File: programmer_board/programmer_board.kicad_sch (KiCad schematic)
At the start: 14 parts, among them J1 8bit_thing_bus_connector, J2 greenpak_i2c, U1 Pico, U2 74AHCT573, U3 74AHCT573, U4 74AHCT573, U5 74LVC245, U6 SLG46826G

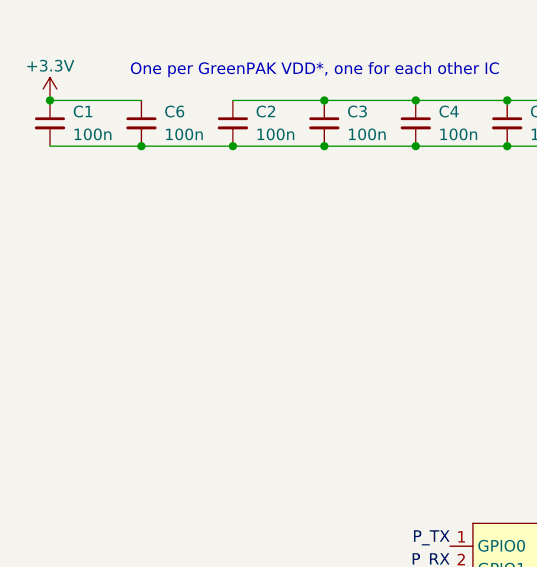
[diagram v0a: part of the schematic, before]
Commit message: pico board: add more bypass caps, add JLCPCB string
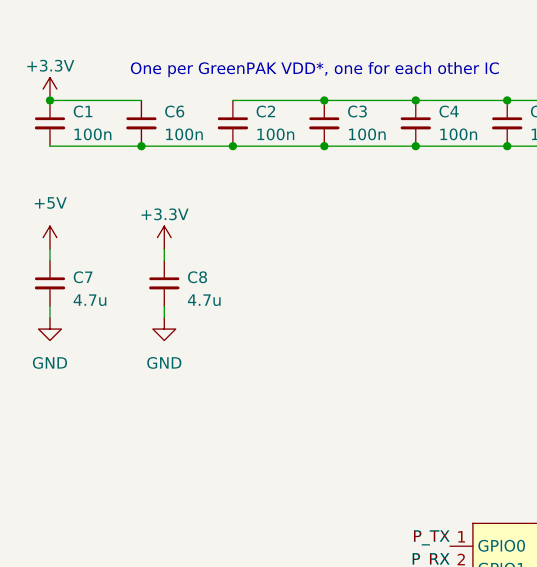
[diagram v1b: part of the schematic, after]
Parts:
- added C7, C8: 4.7u, Capacitor_SMD:C_0805_2012Metric_Pad1.18x1.45mm_HandSolder, symbol Device:C_Small
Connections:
- net +3.3V: now also C8.1
- net +5V: now also C7.1
- net GND: now also C7.2, C8.2
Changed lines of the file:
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@@
+    (stroke (width 0) (type default))
+  )
+  (wire (pts (xy 34.29 50.8) (xy 34.29 49.53))
     (stroke (width 0) (type default))
   )
@@
     (stroke (width 0) (type default))
   )
+  (wire (pts (xy 34.29 43.18) (xy 34.29 44.45))
+    (stroke (width 0) (type default))
+  )
   (wire (pts (xy 236.22 107.95) (xy 241.3 107.95))
     (stroke (width 0) (type default))
@@
     (stroke (width 0) (type default))
   )
+  (wire (pts (xy 21.59 50.8) (xy 21.59 49.53))
+    (stroke (width 0) (type default))
+  )
   (bus (pts (xy 222.25 109.22) (xy 222.25 106.68))
     (stroke (width 0) (type default))
@@
   )
   (wire (pts (xy 236.22 92.71) (xy 241.3 92.71))
+    (stroke (width 0) (type default))
+  )
+  (wire (pts (xy 21.59 43.18) (xy 21.59 44.45))
     (stroke (width 0) (type default))
   )
@@
     )
   )
+  (symbol (lib_id "power:+5V") (at 21.59 43.18 0) (unit 1)
+    (in_bom yes) (on_board yes) (dnp no) (fields_autoplaced)
+    (property "Reference" "#PWR025" (at 21.59 46.99 0)
+      (effects (font (size 1.27 1.27)) hide)
+    )
+    (property "Value" "+5V" (at 21.59 38.1 0)
+      (effects (font (size 1.27 1.27)))
+    )
+    (property "Footprint" "" (at 21.59 43.18 0)
+      (effects (font (size 1.27 1.27)) hide)
+    )
+    (property "Datasheet" "" (at 21.59 43.18 0)
+      (effects (font (size 1.27 1.27)) hide)
+    )
+    (pin "1")
+    (instances
+      (project "programmer_board"
+        (path "/d80ca4e7-5430-4474-aabd-9f00c61eaf5c"
+          (reference "#PWR025") (unit 1)
+        )
+      )
+      (project "HD6301V1_thing"
+        (path "/f94fb884-8365-431c-b8b6-ec4493810111"
+          (reference "#PWR031") (unit 1)
+        )
+      )
+    )
+  )
   (symbol (lib_id "power:GND") (at 203.2 121.92 0) (unit 1)
     (in_bom yes) (on_board yes) (dnp no)
@@
     )
   )
+  (symbol (lib_id "Device:C_Small") (at 21.59 46.99 0) (unit 1)
+    (in_bom yes) (on_board yes) (dnp no) (fields_autoplaced)
+    (property "Reference" "C7" (at 24.13 46.3613 0)
+      (effects (font (size 1.27 1.27)) (justify left))
+    )
+    (property "Value" "4.7u" (at 24.13 48.9013 0)
+      (effects (font (size 1.27 1.27)) (justify left))
+    )
+    (property "Footprint" "Capacitor_SMD:C_0805_2012Metric_Pad1.18x1.45mm_HandSolder" (at 21.59 46.99 0)
+      (effects (font (size 1.27 1.27)) hide)
+    )
+    (property "Datasheet" "~" (at 21.59 46.99 0)
+      (effects (font (size 1.27 1.27)) hide)
+    )
+    (pin "1")
+    (pin "2")
+    (instances
+      (project "programmer_board"
+        (path "/d80ca4e7-5430-4474-aabd-9f00c61eaf5c"
+          (reference "C7") (unit 1)
+        )
+      )
+      (project "HD6301V1_thing"
+        (path "/f94fb884-8365-431c-b8b6-ec4493810111"
+          (reference "C5") (unit 1)
+        )
+      )
+    )
+  )
   (symbol (lib_id "power:GND") (at 180.34 157.48 0) (unit 1)
     (in_bom yes) (on_board yes) (dnp no)
@@
     )
   )
+  (symbol (lib_id "Device:C_Small") (at 34.29 46.99 0) (unit 1)
+    (in_bom yes) (on_board yes) (dnp no) (fields_autoplaced)
+    (property "Reference" "C8" (at 36.83 46.3613 0)
+      (effects (font (size 1.27 1.27)) (justify left))
+    )
+    (property "Value" "4.7u" (at 36.83 48.9013 0)
+      (effects (font (size 1.27 1.27)) (justify left))
+    )
+    (property "Footprint" "Capacitor_SMD:C_0805_2012Metric_Pad1.18x1.45mm_HandSolder" (at 34.29 46.99 0)
+      (effects (font (size 1.27 1.27)) hide)
+    )
+    (property "Datasheet" "~" (at 34.29 46.99 0)
+      (effects (font (size 1.27 1.27)) hide)
+    )
+    (pin "1")
+    (pin "2")
+    (instances
+      (project "programmer_board"
+        (path "/d80ca4e7-5430-4474-aabd-9f00c61eaf5c"
+          (reference "C8") (unit 1)
+        )
+      )
+      (project "HD6301V1_thing"
+        (path "/f94fb884-8365-431c-b8b6-ec4493810111"
+          (reference "C5") (unit 1)
+        )
+      )
+    )
+  )
   (symbol (lib_id "power:GND") (at 154.94 66.04 0) (unit 1)
     (in_bom yes) (on_board yes) (dnp no) (fields_autoplaced)
@@
         (path "/d80ca4e7-5430-4474-aabd-9f00c61eaf5c"
           (reference "#PWR016") (unit 1)
+        )
+      )
+    )
+  )
+  (symbol (lib_id "power:+3.3V") (at 34.29 43.18 0) (unit 1)
+    (in_bom yes) (on_board yes) (dnp no) (fields_autoplaced)
+    (property "Reference" "#PWR024" (at 34.29 46.99 0)
+      (effects (font (size 1.27 1.27)) hide)
+    )
+    (property "Value" "+3.3V" (at 34.29 39.37 0)
+      (effects (font (size 1.27 1.27)))
+    )
+    (property "Footprint" "" (at 34.29 43.18 0)
+      (effects (font (size 1.27 1.27)) hide)
+    )
+    (property "Datasheet" "" (at 34.29 43.18 0)
+      (effects (font (size 1.27 1.27)) hide)
+    )
+    (pin "1")
+    (instances
+      (project "programmer_board"
+        (path "/d80ca4e7-5430-4474-aabd-9f00c61eaf5c"
+          (reference "#PWR024") (unit 1)
         )
       )
@@
     )
   )
+  (symbol (lib_id "power:GND") (at 34.29 50.8 0) (unit 1)
+    (in_bom yes) (on_board yes) (dnp no) (fields_autoplaced)
+    (property "Reference" "#PWR027" (at 34.29 57.15 0)
+      (effects (font (size 1.27 1.27)) hide)
+    )
+    (property "Value" "GND" (at 34.29 55.88 0)
+      (effects (font (size 1.27 1.27)))
+    )
+    (property "Footprint" "" (at 34.29 50.8 0)
+      (effects (font (size 1.27 1.27)) hide)
+    )
+    (property "Datasheet" "" (at 34.29 50.8 0)
+      (effects (font (size 1.27 1.27)) hide)
+    )
+    (pin "1")
+    (instances
+      (project "programmer_board"
+        (path "/d80ca4e7-5430-4474-aabd-9f00c61eaf5c"
+          (reference "#PWR027") (unit 1)
+        )
+      )
+      (project "HD6301V1_thing"
+        (path "/f94fb884-8365-431c-b8b6-ec4493810111"
+          (reference "#PWR032") (unit 1)
+        )
+      )
+    )
+  )
   (symbol (lib_id "power:+5V") (at 104.14 66.04 0) (unit 1)
     (in_bom yes) (on_board yes) (dnp no) (fields_autoplaced)
@@
         )
       )
+    )
+  )
+  (symbol (lib_id "power:GND") (at 21.59 50.8 0) (unit 1)
+    (in_bom yes) (on_board yes) (dnp no) (fields_autoplaced)
+    (property "Reference" "#PWR026" (at 21.59 57.15 0)
+      (effects (font (size 1.27 1.27)) hide)
+    )
+    (property "Value" "GND" (at 21.59 55.88 0)
+      (effects (font (size 1.27 1.27)))
+    )
+    (property "Footprint" "" (at 21.59 50.8 0)
+      (effects (font (size 1.27 1.27)) hide)
+    )
+    (property "Datasheet" "" (at 21.59 50.8 0)
+      (effects (font (size 1.27 1.27)) hide)
+    )
+    (pin "1")
+    (instances
+      (project "programmer_board"
+        (path "/d80ca4e7-5430-4474-aabd-9f00c61eaf5c"
+          (reference "#PWR026") (unit 1)
+        )
+      )
+      (project "HD6301V1_thing"
+        (path "/f94fb884-8365-431c-b8b6-ec4493810111"
+          (reference "#PWR032") (unit 1)
+        )
+      )

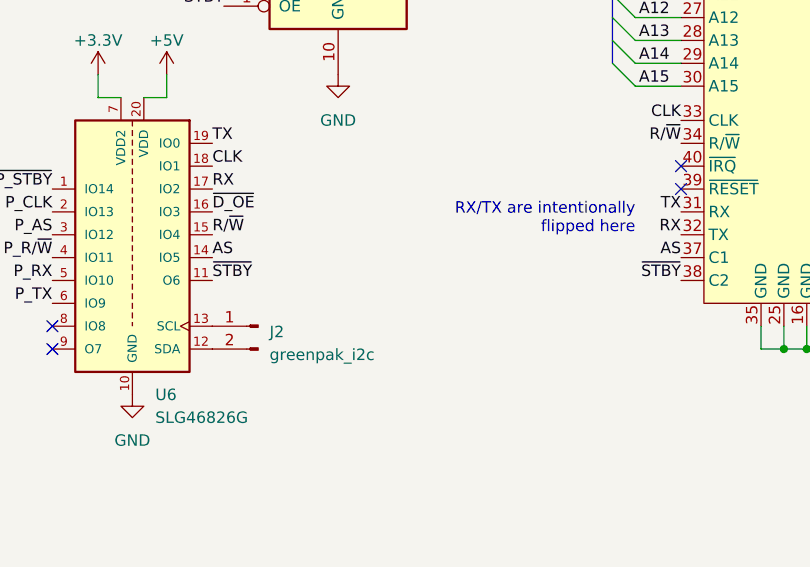
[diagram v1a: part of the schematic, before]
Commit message: Pico board: add i2c pullups
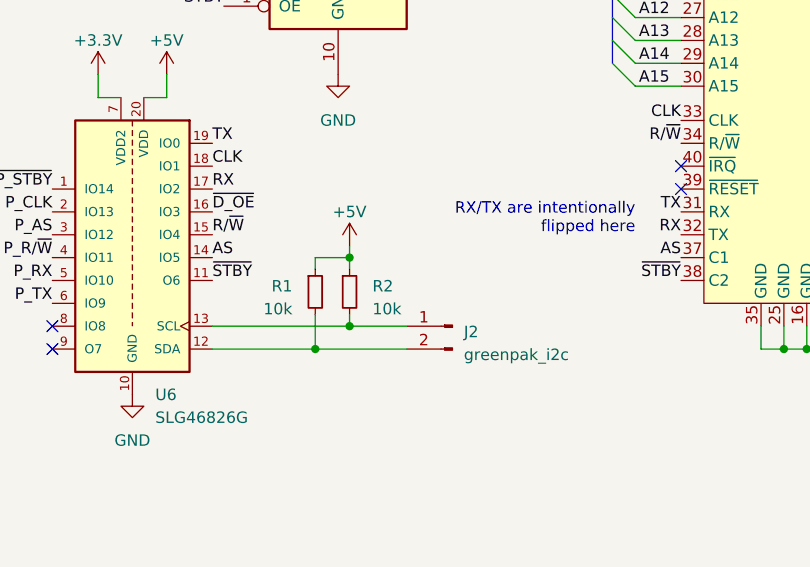
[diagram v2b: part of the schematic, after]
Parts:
- added R1, R2: 10k, Resistor_SMD:R_0805_2012Metric_Pad1.20x1.40mm_HandSolder, symbol Device:R_Small
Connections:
- net +5V: now also R1.1, R2.1
- net at J2.1 (Pin_1), U6.13 (SCL): now also R2.2
- net at J2.2 (Pin_2), U6.12 (SDA): now also R1.2
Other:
- moved on the sheet: J2
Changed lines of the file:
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@@
   (junction (at 110.49 106.68) (diameter 0) (color 0 0 0 0)
   )
+  (junction (at 204.47 142.24) (diameter 0) (color 0 0 0 0)
+  )
   (junction (at 62.23 31.75) (diameter 0) (color 0 0 0 0)
   )
@@
   (junction (at 257.81 152.4) (diameter 0) (color 0 0 0 0)
   )
+  (junction (at 204.47 149.86) (diameter 0) (color 0 0 0 0)
+  )
   (junction (at 52.07 31.75) (diameter 0) (color 0 0 0 0)
   )
   (junction (at 110.49 93.98) (diameter 0) (color 0 0 0 0)
+  )
+  (junction (at 200.66 152.4) (diameter 0) (color 0 0 0 0)
   )
   (junction (at 72.39 31.75) (diameter 0) (color 0 0 0 0)
@@
     (stroke (width 0) (type default))
   )
+  (wire (pts (xy 200.66 142.24) (xy 204.47 142.24))
+    (stroke (width 0) (type default))
+  )
   (wire (pts (xy 236.22 66.04) (xy 241.3 66.04))
     (stroke (width 0) (type default))
@@
     (stroke (width 0) (type default))
   )
+  (wire (pts (xy 204.47 148.59) (xy 204.47 149.86))
+    (stroke (width 0) (type default))
+  )
   (wire (pts (xy 48.26 119.38) (xy 48.26 130.81))
     (stroke (width 0) (type default))
   )
+  (wire (pts (xy 204.47 142.24) (xy 204.47 143.51))
+    (stroke (width 0) (type default))
+  )
   (wire (pts (xy 139.7 57.15) (xy 142.24 57.15))
     (stroke (width 0) (type default))
@@
     (stroke (width 0) (type default))
   )
+  (wire (pts (xy 200.66 143.51) (xy 200.66 142.24))
+    (stroke (width 0) (type default))
+  )
   (wire (pts (xy 104.14 78.74) (xy 104.14 76.2))
     (stroke (width 0) (type default))
@@
     (stroke (width 0) (type default))
   )
+  (wire (pts (xy 210.82 149.86) (xy 204.47 149.86))
+    (stroke (width 0) (type default))
+  )
   (bus (pts (xy 173.99 106.68) (xy 173.99 104.14))
     (stroke (width 0) (type default))
@@
     (stroke (width 0) (type default))
   )
+  (wire (pts (xy 210.82 152.4) (xy 200.66 152.4))
+    (stroke (width 0) (type default))
+  )
   (wire (pts (xy 236.22 78.74) (xy 241.3 78.74))
     (stroke (width 0) (type default))
@@
     (stroke (width 0) (type default))
   )
+  (wire (pts (xy 200.66 152.4) (xy 189.23 152.4))
+    (stroke (width 0) (type default))
+  )
   (bus (pts (xy 233.68 115.57) (xy 233.68 118.11))
     (stroke (width 0) (type default))
@@
     (stroke (width 0) (type default))
   )
+  (wire (pts (xy 200.66 148.59) (xy 200.66 152.4))
+    (stroke (width 0) (type default))
+  )
   (wire (pts (xy 219.71 99.06) (xy 215.9 99.06))
     (stroke (width 0) (type default))
@@
     (stroke (width 0) (type default))
   )
+  (wire (pts (xy 204.47 149.86) (xy 189.23 149.86))
+    (stroke (width 0) (type default))
+  )
   (wire (pts (xy 171.45 41.91) (xy 167.64 41.91))
     (stroke (width 0) (type default))
@@
   )
   (wire (pts (xy 48.26 106.68) (xy 48.26 119.38))
+    (stroke (width 0) (type default))
+  )
+  (wire (pts (xy 204.47 140.97) (xy 204.47 142.24))
     (stroke (width 0) (type default))
   )
@@
     )
   )
-  (symbol (lib_id "Connector:Conn_01x02_Pin") (at 194.31 149.86 0) (mirror y) (unit 1)
+  (symbol (lib_id "Connector:Conn_01x02_Pin") (at 215.9 149.86 0) (mirror y) (unit 1)
     (in_bom yes) (on_board yes) (dnp no)
-    (property "Reference" "J2" (at 195.58 150.495 0)
+    (property "Reference" "J2" (at 217.17 150.495 0)
       (effects (font (size 1.27 1.27)) (justify right))
     )
-    (property "Value" "greenpak_i2c" (at 195.58 153.035 0)
+    (property "Value" "greenpak_i2c" (at 217.17 153.035 0)
       (effects (font (size 1.27 1.27)) (justify right))
     )
-    (property "Footprint" "own_footprints:PinHeader_1x02_P2.54mm_Vertical_minimal" (at 194.31 149.86 0)
-      (effects (font (size 1.27 1.27)) hide)
-    )
-    (property "Datasheet" "~" (at 194.31 149.86 0)
+    (property "Footprint" "own_footprints:PinHeader_1x02_P2.54mm_Vertical_minimal" (at 215.9 149.86 0)
+      (effects (font (size 1.27 1.27)) hide)
+    )
+    (property "Datasheet" "~" (at 215.9 149.86 0)
       (effects (font (size 1.27 1.27)) hide)
     )
@@
     )
   )
+  (symbol (lib_id "Device:R_Small") (at 200.66 146.05 0) (unit 1)
+    (in_bom yes) (on_board yes) (dnp no) (fields_autoplaced)
+    (property "Reference" "R1" (at 198.12 145.415 0)
+      (effects (font (size 1.27 1.27)) (justify right))
+    )
+    (property "Value" "10k" (at 198.12 147.955 0)
+      (effects (font (size 1.27 1.27)) (justify right))
+    )
+    (property "Footprint" "Resistor_SMD:R_0805_2012Metric_Pad1.20x1.40mm_HandSolder" (at 200.66 146.05 0)
+      (effects (font (size 1.27 1.27)) hide)
+    )
+    (property "Datasheet" "~" (at 200.66 146.05 0)
+      (effects (font (size 1.27 1.27)) hide)
+    )
+    (pin "1")
+    (pin "2")
+    (instances
+      (project "programmer_board"
+        (path "/d80ca4e7-5430-4474-aabd-9f00c61eaf5c"
+          (reference "R1") (unit 1)
+        )
+      )
+    )
+  )
   (symbol (lib_id "power:GND") (at 83.82 33.02 0) (unit 1)
     (in_bom yes) (on_board yes) (dnp no) (fields_autoplaced)
@@
         (path "/d80ca4e7-5430-4474-aabd-9f00c61eaf5c"
           (reference "#PWR07") (unit 1)
+        )
+      )
+    )
+  )
+  (symbol (lib_id "Device:R_Small") (at 204.47 146.05 0) (unit 1)
+    (in_bom yes) (on_board yes) (dnp no) (fields_autoplaced)
+    (property "Reference" "R2" (at 207.01 145.415 0)
+      (effects (font (size 1.27 1.27)) (justify left))
+    )
+    (property "Value" "10k" (at 207.01 147.955 0)
+      (effects (font (size 1.27 1.27)) (justify left))
+    )
+    (property "Footprint" "Resistor_SMD:R_0805_2012Metric_Pad1.20x1.40mm_HandSolder" (at 204.47 146.05 0)
+      (effects (font (size 1.27 1.27)) hide)
+    )
+    (property "Datasheet" "~" (at 204.47 146.05 0)
+      (effects (font (size 1.27 1.27)) hide)
+    )
+    (pin "1")
+    (pin "2")
+    (instances
+      (project "programmer_board"
+        (path "/d80ca4e7-5430-4474-aabd-9f00c61eaf5c"
+          (reference "R2") (unit 1)
         )
       )
@@
         )
       )
+    )
+  )
+  (symbol (lib_id "power:+5V") (at 204.47 140.97 0) (mirror y) (unit 1)
+    (in_bom yes) (on_board yes) (dnp no) (fields_autoplaced)
+    (property "Reference" "#PWR028" (at 204.47 144.78 0)
+      (effects (font (size 1.27 1.27)) hide)
+    )
+    (property "Value" "+5V" (at 204.47 137.16 0)
+      (effects (font (size 1.27 1.27)))
+    )
+    (property "Footprint" "" (at 204.47 140.97 0)
+      (effects (font (size 1.27 1.27)) hide)
+    )
+    (property "Datasheet" "" (at 204.47 140.97 0)
+      (effects (font (size 1.27 1.27)) hide)
+    )
+    (pin "1")
+    (instances
+      (project "programmer_board"
+        (path "/d80ca4e7-5430-4474-aabd-9f00c61eaf5c"
+          (reference "#PWR028") (unit 1)
+        )
+      )
